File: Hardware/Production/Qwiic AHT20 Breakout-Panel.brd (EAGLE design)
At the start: 149.1 x 149.1 mm, 980 parts, among them J1 QWIIC_RIGHT_ANGLE, J10 QWIIC_RIGHT_ANGLE, J11 PTH, J12 QWIIC_RIGHT_ANGLE, J13 QWIIC_RIGHT_ANGLE, J14 PTH, J15 QWIIC_RIGHT_ANGLE, J16 QWIIC_RIGHT_ANGLE, J17 PTH, J18 QWIIC_RIGHT_ANGLE, J19 QWIIC_RIGHT_ANGLE, J2 QWIIC_RIGHT_ANGLE, J20 PTH, J21 QWIIC_RIGHT_ANGLE, J22 QWIIC_RIGHT_ANGLE, J23 PTH, J24 QWIIC_RIGHT_ANGLE, J25 QWIIC_RIGHT_ANGLE, J26 PTH, J27 QWIIC_RIGHT_ANGLE, J28 QWIIC_RIGHT_ANGLE, J29 PTH, J3 PTH, J30 QWIIC_RIGHT_ANGLE, J31 QWIIC_RIGHT_ANGLE, J32 PTH, J33 QWIIC_RIGHT_ANGLE, J34 QWIIC_RIGHT_ANGLE, J35 PTH, J36 QWIIC_RIGHT_ANGLE, J37 QWIIC_RIGHT_ANGLE, J38 PTH, J39 QWIIC_RIGHT_ANGLE, J4 QWIIC_RIGHT_ANGLE, J40 QWIIC_RIGHT_ANGLE, J41 PTH, J42 QWIIC_RIGHT_ANGLE, J43 QWIIC_RIGHT_ANGLE, J44 PTH, J45 QWIIC_RIGHT_ANGLE, J46 QWIIC_RIGHT_ANGLE, J47 PTH, J48 QWIIC_RIGHT_ANGLE, J49 QWIIC_RIGHT_ANGLE, J5 PTH, J50 PTH, J51 QWIIC_RIGHT_ANGLE, J52 QWIIC_RIGHT_ANGLE, J53 PTH, J54 QWIIC_RIGHT_ANGLE, J55 QWIIC_RIGHT_ANGLE, J56 PTH, J57 QWIIC_RIGHT_ANGLE, J58 QWIIC_RIGHT_ANGLE, J59 PTH, J6 QWIIC_RIGHT_ANGLE, J60 QWIIC_RIGHT_ANGLE, J61 QWIIC_RIGHT_ANGLE, J62 PTH, J63 QWIIC_RIGHT_ANGLE, J64 QWIIC_RIGHT_ANGLE, J65 PTH, J66 QWIIC_RIGHT_ANGLE, J67 QWIIC_RIGHT_ANGLE, J68 PTH, J69 QWIIC_RIGHT_ANGLE, J7 QWIIC_RIGHT_ANGLE, J70 QWIIC_RIGHT_ANGLE, J71 PTH, J72 QWIIC_RIGHT_ANGLE, J73 QWIIC_RIGHT_ANGLE, J74 PTH, J75 QWIIC_RIGHT_ANGLE, J8 PTH, J9 QWIIC_RIGHT_ANGLE, U1 AHT20QFN-6, U10 AHT20QFN-6, U11 AHT20QFN-6, U12 AHT20QFN-6, U13 AHT20QFN-6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

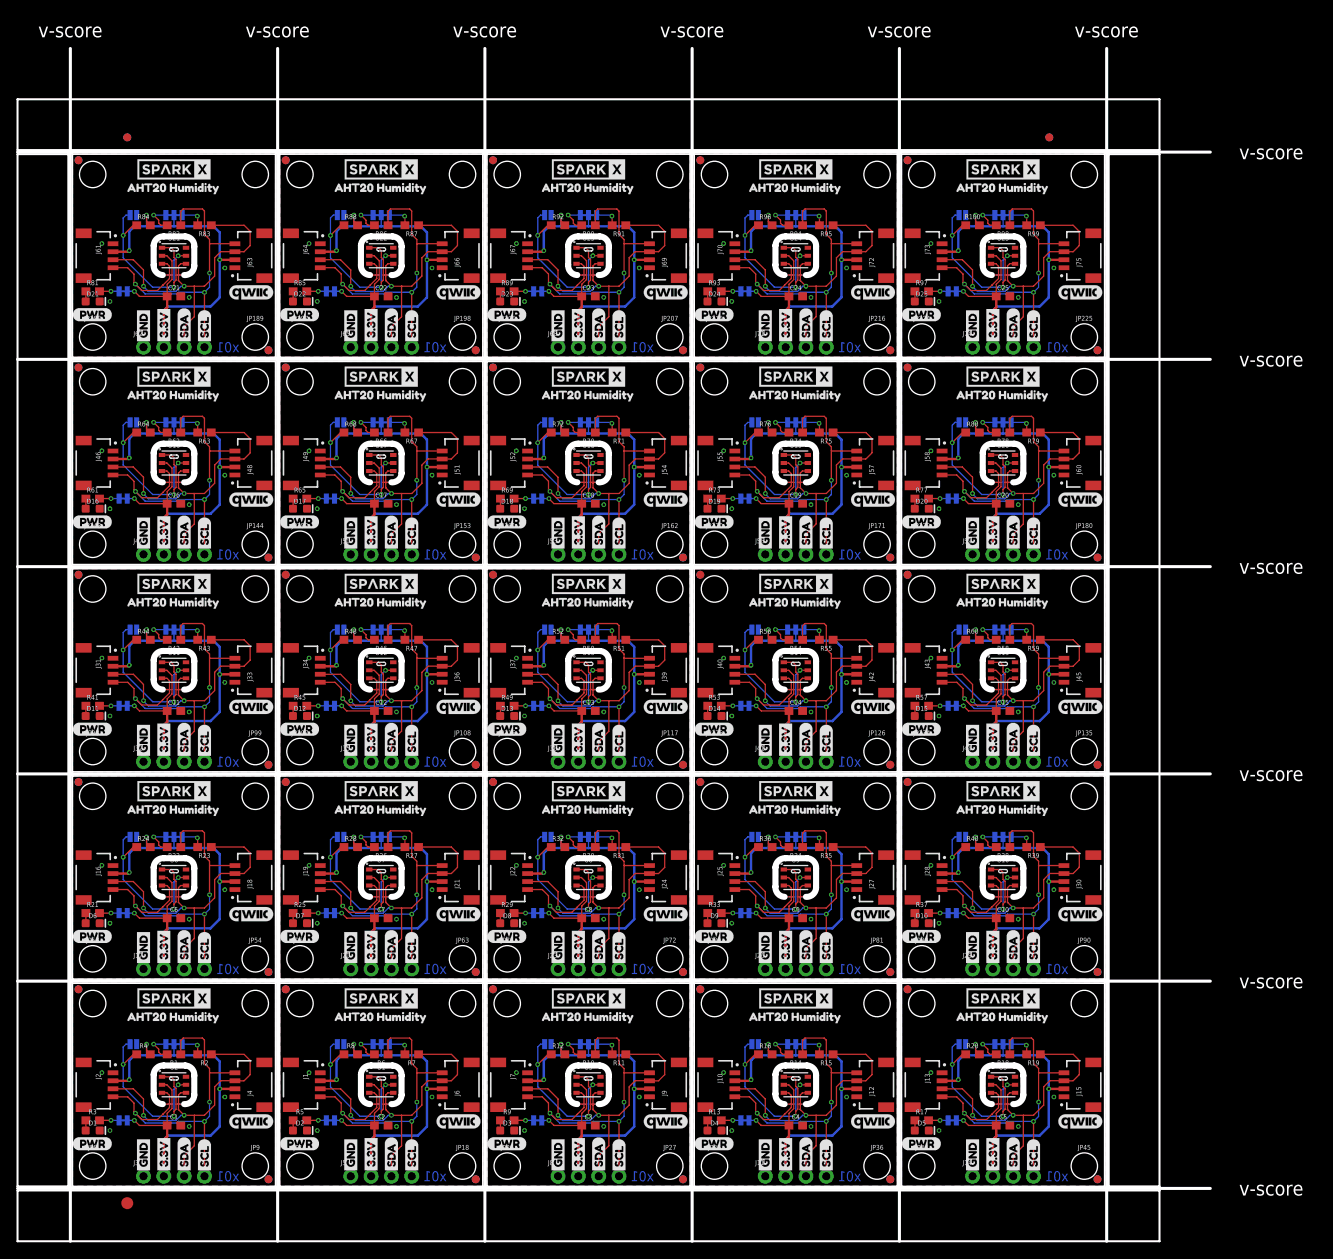
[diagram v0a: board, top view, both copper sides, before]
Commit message: Fix FP spacing. Remove experimental ADR feature. Update version number.
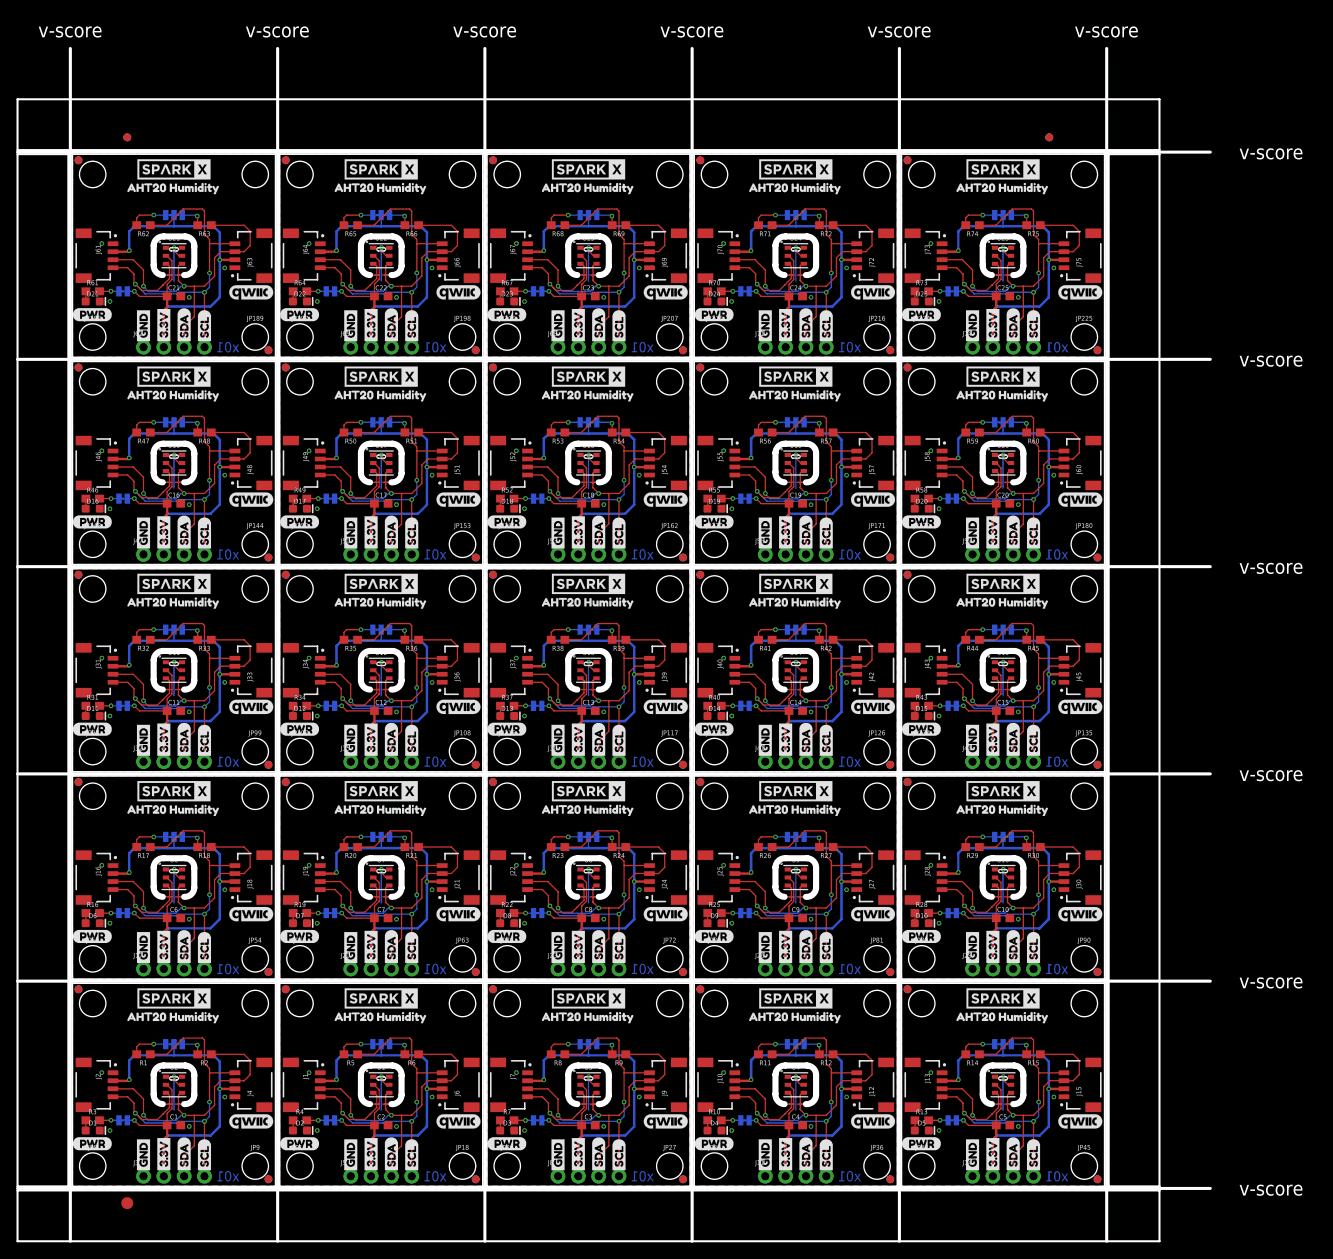
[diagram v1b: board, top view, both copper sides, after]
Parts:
- removed ADR, ADR1, ADR10, ADR11, ADR12, ADR13, ADR14, ADR15, ADR16, ADR17, ADR18, ADR19, ADR2, ADR20, ADR21, ADR22, ADR23, ADR24, ADR3, ADR4, ADR5, ADR6, ADR7, ADR8, ADR9: (no value), SparkFun-Jumpers:SMT-JUMPER_2_NO_SILK
- removed R100, R76, R80, R84, R88, R92, R96: 10k, SparkFun-Resistors:0603
- removed R77, R81, R85, R89, R93, R97: 1k, SparkFun-Resistors:0603
- removed R78, R79, R82, R83, R86, R87, R90, R91, R94, R95, R98, R99: 2.2k, SparkFun-Resistors:0603
- removed U$401, U$413, U$418: (no value), Labels-0_04:SCL9
- removed U$402, U$419: (no value), Labels-0_04:(PWR)
- removed U$403, U$420: (no value), Labels:I_SUPER2_C-()-03
- removed U$404, U$421: (no value), SparkFun-Aesthetics:QWIIC_5.5MM
- removed U$405, U$422: (no value), Labels:ADR-()-03
- removed U$406, U$408, U$423, U$425: (no value), buzzard_labels (17):AHT20_HUMIDITY2
- removed U$407, U$424: (no value), SparkFun-Buzzard:LED_32
- removed U$409, U$410: SPARKX-LOGO4, SparkX:SPARKX-MEDIUM
- removed U$411, U$416: (no value), Labels-0_04:3#3V2
- removed U$412, U$415: (no value), Labels-0_04:GND1
- removed U$414, U$417: (no value), Labels-0_04:SDA8
- LED, LED1, LED10, LED11, LED12, LED13, LED14, LED15, LED16, LED17, LED18, LED19, LED2, LED20, LED21, LED22, LED23, LED24, LED3, LED4, LED5, LED6, LED7, LED8, LED9: value (none) -> JUMPER-SMT_2_NC_TRACE_SILK
- R10, R19, R22, R31, R34, R43, R46, R55, R58, R67, R7, R70: value 2.2k -> 1k
- R12, R20, R24, R32, R36, R44, R48, R56, R60, R68, R72, R8: value 10k -> 2.2k
- R16, R28, R4, R40, R52, R64: value 10k -> 1k
- R17, R21, R29, R33, R41, R45, R5, R53, R57, R65, R69, R9: value 1k -> 2.2k
- U$100, U$119, U$151, U$340, U$372, U$391, U$68: device buzzard_labels (17):AHT20_HUMIDITY2 -> Labels-0_04:GND1
- U$101, U$186, U$373: device SparkFun-Buzzard:LED_32 -> Labels-0_04:SCL9
- U$102, U$134, U$153, U$185, U$374: device buzzard_labels (17):AHT20_HUMIDITY2 -> Labels-0_04:SDA8
- U$103, U$308, U$324, U$359, U$36, U$375, U$52, U$87: value SPARKX-LOGO4 -> (none); device SparkX:SPARKX-MEDIUM -> Labels-0_04:GND1
- U$104, U$120, U$15, U$291, U$307, U$35, U$376, U$392: value SPARKX-LOGO4 -> (none); device SparkX:SPARKX-MEDIUM -> Labels-0_04:3#3V2
- U$105, U$23, U$246, U$297, U$326, U$377, U$54: device Labels-0_04:3#3V2 -> Labels-0_04:SDA8
- U$106, U$17, U$245, U$293, U$330, U$378, U$58: device Labels-0_04:GND1 -> Labels-0_04:SCL9
- U$107, U$25, U$299, U$379: device Labels-0_04:SCL9 -> Labels-0_04:(PWR)
- U$108, U$332, U$380, U$60: device Labels-0_04:SDA8 -> Labels:I_SUPER2_C-()-03
- U$109, U$157, U$381: device Labels-0_04:GND1 -> SparkFun-Aesthetics:QWIIC_5.5MM
- U$110, U$144, U$190, U$224, U$382: device Labels-0_04:3#3V2 -> buzzard_labels (17):AHT20_HUMIDITY2
- U$111, U$159, U$383: device Labels-0_04:SDA8 -> SparkFun-Buzzard:LED_32
- U$112, U$158, U$192, U$350, U$384, U$78: device Labels-0_04:SCL9 -> buzzard_labels (17):AHT20_HUMIDITY2
- U$113, U$130, U$385: value (none) -> SPARKX-LOGO4; device Labels-0_04:(PWR) -> SparkX:SPARKX-MEDIUM
- U$114, U$369, U$386, U$97: value (none) -> SPARKX-LOGO4; device Labels:I_SUPER2_C-()-03 -> SparkX:SPARKX-MEDIUM
- U$115, U$200, U$387: device SparkFun-Aesthetics:QWIIC_5.5MM -> Labels-0_04:3#3V2
- U$116, U$167, U$388: device Labels:ADR-()-03 -> Labels-0_04:GND1
- U$117, U$170, U$202, U$357, U$389, U$85: device buzzard_labels (17):AHT20_HUMIDITY2 -> Labels-0_04:SCL9
- U$118, U$169, U$390: device SparkFun-Buzzard:LED_32 -> Labels-0_04:SDA8
- U$121, U$137, U$342, U$358, U$393, U$70, U$86: value SPARKX-LOGO4 -> (none); device SparkX:SPARKX-MEDIUM -> Labels-0_04:SDA8
- U$122, U$229, U$309, U$314, U$37, U$394, U$42: device Labels-0_04:3#3V2 -> Labels-0_04:SCL9
- U$123, U$347, U$395, U$75: device Labels-0_04:GND1 -> Labels-0_04:(PWR)
- U$124, U$316, U$396, U$44: device Labels-0_04:SCL9 -> Labels:I_SUPER2_C-()-03
- U$125, U$349, U$397, U$77: device Labels-0_04:SDA8 -> SparkFun-Aesthetics:QWIIC_5.5MM
- U$126, U$160, U$174, U$208, U$398: device Labels-0_04:GND1 -> buzzard_labels (17):AHT20_HUMIDITY2
- U$127, U$207, U$399: device Labels-0_04:3#3V2 -> SparkFun-Buzzard:LED_32
- U$128, U$142, U$176, U$366, U$400, U$94: device Labels-0_04:SDA8 -> buzzard_labels (17):AHT20_HUMIDITY2
- U$129, U$146, U$209, U$226: value (none) -> SPARKX-LOGO4; device Labels-0_04:SCL9 -> SparkX:SPARKX-MEDIUM
- U$13, U$337, U$354, U$65, U$82: value (none) -> SPARKX-LOGO4; device Labels:ADR-()-03 -> SparkX:SPARKX-MEDIUM
- U$131, U$216: device Labels:I_SUPER2_C-()-03 -> Labels-0_04:3#3V2
- U$132, U$183: device SparkFun-Aesthetics:QWIIC_5.5MM -> Labels-0_04:GND1
- U$133, U$218: device Labels:ADR-()-03 -> Labels-0_04:SCL9
- U$135, U$356, U$84: device SparkFun-Buzzard:LED_32 -> Labels-0_04:GND1
- U$136, U$168, U$323, U$355, U$51, U$83: device buzzard_labels (17):AHT20_HUMIDITY2 -> Labels-0_04:3#3V2
- U$138, U$154, U$325, U$341, U$53, U$69: value SPARKX-LOGO4 -> (none); device SparkX:SPARKX-MEDIUM -> Labels-0_04:SCL9
- U$139, U$331, U$59: device Labels-0_04:3#3V2 -> Labels-0_04:(PWR)
- U$140, U$364, U$92: device Labels-0_04:GND1 -> Labels:I_SUPER2_C-()-03
- U$141, U$333, U$61: device Labels-0_04:SCL9 -> SparkFun-Aesthetics:QWIIC_5.5MM
- U$143, U$191: device Labels-0_04:GND1 -> SparkFun-Buzzard:LED_32
- U$145, U$162, U$193, U$210: value (none) -> SPARKX-LOGO4; device Labels-0_04:SDA8 -> SparkX:SPARKX-MEDIUM
- U$147, U$232: device Labels-0_04:(PWR) -> Labels-0_04:3#3V2
- U$148, U$199: device Labels:I_SUPER2_C-()-03 -> Labels-0_04:GND1
- U$149, U$234: device SparkFun-Aesthetics:QWIIC_5.5MM -> Labels-0_04:SCL9
- U$150, U$201: device Labels:ADR-()-03 -> Labels-0_04:SDA8
- U$152, U$339, U$67: device SparkFun-Buzzard:LED_32 -> Labels-0_04:3#3V2
- U$155, U$171: value SPARKX-LOGO4 -> (none); device SparkX:SPARKX-MEDIUM -> Labels-0_04:(PWR)
- U$156, U$348, U$76: device Labels-0_04:3#3V2 -> Labels:I_SUPER2_C-()-03
- U$16, U$212, U$263, U$292, U$343, U$71: device Labels-0_04:3#3V2 -> Labels-0_04:GND1
- U$161, U$178, U$241, U$258: value (none) -> SPARKX-LOGO4; device Labels-0_04:3#3V2 -> SparkX:SPARKX-MEDIUM
- U$163, U$243, U$248, U$328, U$56: device Labels-0_04:SCL9 -> Labels-0_04:3#3V2
- U$164, U$215: device Labels-0_04:(PWR) -> Labels-0_04:GND1
- U$165, U$250: device Labels:I_SUPER2_C-()-03 -> Labels-0_04:SCL9
- U$166, U$217: device SparkFun-Aesthetics:QWIIC_5.5MM -> Labels-0_04:SDA8
- U$172, U$188: value SPARKX-LOGO4 -> (none); device SparkX:SPARKX-MEDIUM -> Labels:I_SUPER2_C-()-03
- U$173, U$365, U$93: device Labels-0_04:3#3V2 -> SparkFun-Aesthetics:QWIIC_5.5MM
- U$175, U$367, U$95: device Labels-0_04:SCL9 -> SparkFun-Buzzard:LED_32
- U$177, U$194, U$225, U$242: value (none) -> SPARKX-LOGO4; device Labels-0_04:GND1 -> SparkX:SPARKX-MEDIUM
- U$179, U$227, U$264, U$312, U$40: device Labels-0_04:SDA8 -> Labels-0_04:3#3V2
- U$18, U$214, U$265, U$294, U$345, U$73: device Labels-0_04:SCL9 -> Labels-0_04:SDA8
- U$180, U$231, U$260, U$311, U$39: device Labels-0_04:SCL9 -> Labels-0_04:GND1
- U$181, U$266: device Labels-0_04:(PWR) -> Labels-0_04:SCL9
- U$182, U$233: device Labels:I_SUPER2_C-()-03 -> Labels-0_04:SDA8
- U$184, U$371, U$99: device Labels:ADR-()-03 -> Labels-0_04:3#3V2
- U$187, U$219: device buzzard_labels (17):AHT20_HUMIDITY2 -> Labels-0_04:(PWR)
- U$189, U$205: value SPARKX-LOGO4 -> (none); device SparkX:SPARKX-MEDIUM -> SparkFun-Aesthetics:QWIIC_5.5MM
- U$19, U$196, U$244, U$247, U$295: device Labels-0_04:SDA8 -> Labels-0_04:GND1
- U$198, U$249: device Labels-0_04:(PWR) -> Labels-0_04:SDA8
- U$20, U$211, U$259, U$296, U$344, U$72: device Labels-0_04:GND1 -> Labels-0_04:3#3V2
- U$203: device SparkFun-Buzzard:LED_32 -> Labels-0_04:(PWR)
- U$204, U$236: device buzzard_labels (17):AHT20_HUMIDITY2 -> Labels:I_SUPER2_C-()-03
- U$206, U$222, U$240, U$256: value SPARKX-LOGO4 -> (none); device SparkX:SPARKX-MEDIUM -> buzzard_labels (17):AHT20_HUMIDITY2
- U$213, U$24, U$261, U$298, U$346, U$74: device Labels-0_04:SDA8 -> Labels-0_04:SCL9
- U$220: device SparkFun-Buzzard:LED_32 -> Labels:I_SUPER2_C-()-03
- U$221, U$253: device buzzard_labels (17):AHT20_HUMIDITY2 -> SparkFun-Aesthetics:QWIIC_5.5MM
- U$223, U$239: value SPARKX-LOGO4 -> (none); device SparkX:SPARKX-MEDIUM -> SparkFun-Buzzard:LED_32
- U$235: device Labels:ADR-()-03 -> Labels-0_04:(PWR)
- U$237: device SparkFun-Buzzard:LED_32 -> SparkFun-Aesthetics:QWIIC_5.5MM
- U$251: device SparkFun-Aesthetics:QWIIC_5.5MM -> Labels-0_04:(PWR)
- U$252: device Labels:ADR-()-03 -> Labels:I_SUPER2_C-()-03
- U$254, U$288: device SparkFun-Buzzard:LED_32 -> buzzard_labels (17):AHT20_HUMIDITY2
- U$255, U$287: device buzzard_labels (17):AHT20_HUMIDITY2 -> SparkFun-Buzzard:LED_32
- U$262, U$310, U$313, U$361, U$38, U$41, U$89: device Labels-0_04:GND1 -> Labels-0_04:SDA8
- U$267: device Labels:I_SUPER2_C-()-03 -> Labels-0_04:(PWR)
- U$268: device SparkFun-Aesthetics:QWIIC_5.5MM -> Labels:I_SUPER2_C-()-03
- U$269: device Labels:ADR-()-03 -> SparkFun-Aesthetics:QWIIC_5.5MM
- U$28, U$300: device Labels-0_04:(PWR) -> Labels:I_SUPER2_C-()-03
- U$286, U$320, U$48: device Labels:ADR-()-03 -> buzzard_labels (17):AHT20_HUMIDITY2
- U$289, U$306, U$321, U$338, U$34, U$49, U$66: value (none) -> SPARKX-LOGO4; device buzzard_labels (17):AHT20_HUMIDITY2 -> SparkX:SPARKX-MEDIUM
- U$29, U$301: device Labels:I_SUPER2_C-()-03 -> SparkFun-Aesthetics:QWIIC_5.5MM
- U$30, U$302, U$336, U$64: device SparkFun-Aesthetics:QWIIC_5.5MM -> buzzard_labels (17):AHT20_HUMIDITY2
- U$303, U$31: device Labels:ADR-()-03 -> SparkFun-Buzzard:LED_32
- U$305, U$322, U$33, U$50: value (none) -> SPARKX-LOGO4; device SparkFun-Buzzard:LED_32 -> SparkX:SPARKX-MEDIUM
- U$315, U$363, U$43, U$91: device Labels-0_04:SDA8 -> Labels-0_04:(PWR)
- U$317, U$45: device Labels-0_04:(PWR) -> SparkFun-Aesthetics:QWIIC_5.5MM
- U$318, U$352, U$46, U$80: device Labels:I_SUPER2_C-()-03 -> buzzard_labels (17):AHT20_HUMIDITY2
- U$319, U$47: device SparkFun-Aesthetics:QWIIC_5.5MM -> SparkFun-Buzzard:LED_32
- U$334, U$368, U$62, U$96: device Labels-0_04:(PWR) -> buzzard_labels (17):AHT20_HUMIDITY2
- U$335, U$63: device Labels:I_SUPER2_C-()-03 -> SparkFun-Buzzard:LED_32
- U$351, U$79: device Labels-0_04:(PWR) -> SparkFun-Buzzard:LED_32
- U$353, U$370, U$81, U$98: value (none) -> SPARKX-LOGO4; device SparkFun-Aesthetics:QWIIC_5.5MM -> SparkX:SPARKX-MEDIUM
- moved U$251 128.1 mm to (0.00, 83.1)
- moved U$81 120.6 mm to (12.7, 49.4), flipped to the bottom
- moved U$331 118.8 mm to (0.00, 109.0), flipped to the top, turned to 0 degrees
- moved U$255 115.3 mm to (8.13, 83.9)
- moved U$162 115.3 mm to (12.7, 75.3), flipped to the top, turned to 0 degrees
- moved U$166 113.7 mm to (14.0, 53.3), turned to 90 degrees
- moved U$336 113.6 mm to (19.3, 124.8), flipped to the bottom
- moved U$254 113.4 mm to (5.97, 98.9), flipped to the top
- moved U$161 113.0 mm to (12.7, 75.3), turned to 0 degrees
- moved U$241 113.0 mm to (12.7, 101.2), flipped to the bottom, turned to 0 degrees
- moved U$332 112.5 mm to (14.1, 123.3), turned to 0 degrees
- moved U$244 111.8 mm to (8.89, 79.2)
- moved U$247 111.8 mm to (8.89, 79.2)
- moved U$163 111.8 mm to (11.4, 53.3), flipped to the top
- moved U$243 111.8 mm to (11.4, 79.2)
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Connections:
- removed net N$10: LED1.1, R5.2
- removed net N$100: LED16.1, R65.2
- removed net N$105: JP160.1, R71.2
- removed net N$110: JP169.3, R74.2
- removed net N$115: D20.A, R77.1
- removed net N$125: ADR20.2, R84.1, U21.ADR
- removed net N$127: D22.A, R85.1
- removed net N$128: JP196.3, R86.2
- removed net N$129: JP196.1, R87.2
- removed net N$130: LED21.1, R85.2
- removed net N$131: ADR21.2, R88.1, U22.ADR
- removed net N$133: D23.A, R89.1
- removed net N$134: JP205.3, R90.2
- removed net N$135: JP205.1, R91.2
- removed net N$136: LED22.1, R89.2
- removed net N$137: ADR22.2, R92.1, U23.ADR
- removed net N$139: D24.A, R93.1
- removed net N$140: JP214.3, R94.2
- removed net N$141: JP214.1, R95.2
- removed net N$142: LED23.1, R93.2
- removed net N$143: ADR23.2, R96.1, U24.ADR
- removed net N$145: D25.A, R97.1
- removed net N$146: JP223.3, R98.2
- removed net N$147: JP223.1, R99.2
- removed net N$148: LED24.1, R97.2
- removed net N$149: ADR24.2, R100.1, U25.ADR
- removed net N$15: JP25.1, R11.2
- removed net N$20: JP34.3, R14.2
- removed net N$25: D5.A, R17.1
- removed net N$35: ADR5.2, R24.1, U6.ADR
- removed net N$40: LED6.1, R25.2
- removed net N$45: JP70.1, R31.2
- removed net N$50: JP79.3, R34.2
- removed net N$55: D10.A, R37.1
- removed net N$65: ADR10.2, R44.1, U11.ADR
- removed net N$70: LED11.1, R45.2
- removed net N$75: JP115.1, R51.2
- removed net N$80: JP124.3, R54.2
- removed net N$85: D15.A, R57.1
- removed net N$95: ADR15.2, R64.1, U16.ADR
- new net N$102: JP187.3, R62.2
- new net N$108: JP196.1, R66.2
- new net N$114: LED22.1, R67.2
- new net N$12: JP25.3, R8.2
- new net N$18: JP34.1, R12.2
- new net N$24: LED4.1, R13.2
- new net N$36: D8.A, R22.1
- new net N$42: JP79.3, R26.2
- new net N$48: JP88.1, R30.2
- new net N$54: LED10.1, R31.2
- new net N$66: D14.A, R40.1
- new net N$72: JP133.3, R44.2
- new net N$78: JP142.1, R48.2
- new net N$84: LED16.1, R49.2
- new net N$96: D20.A, R58.1
- net 3.3V: no longer R4.2
- net 3.3V1: no longer R8.2
- net 3.3V10: no longer R44.2
- net 3.3V11: no longer R48.2
- net 3.3V12: no longer R52.2
- net 3.3V13: no longer R56.2
- net 3.3V14: no longer R60.2
- net 3.3V15: no longer R64.2
- net 3.3V16: no longer R68.2
- net 3.3V17: no longer R72.2
- net 3.3V18: no longer R76.2
- net 3.3V19: no longer R80.2
- net 3.3V2: no longer R12.2
- net 3.3V20: no longer R84.2
- net 3.3V21: no longer R88.2
- net 3.3V22: no longer R92.2
- net 3.3V23: no longer R96.2
- net 3.3V24: no longer R100.2
- net 3.3V3: no longer R16.2
- net 3.3V4: no longer R20.2
- net 3.3V5: no longer R24.2
- net 3.3V6: no longer R28.2
- net 3.3V7: no longer R32.2
- net 3.3V8: no longer R36.2
- net 3.3V9: no longer R40.2
- net GND: no longer ADR.1
- net GND1: no longer ADR1.1
- net GND10: no longer ADR10.1
- net GND11: no longer ADR11.1
- net GND12: no longer ADR12.1
- net GND13: no longer ADR13.1
- net GND14: no longer ADR14.1
- net GND15: no longer ADR15.1
- net GND16: no longer ADR16.1
- net GND17: no longer ADR17.1
- net GND18: no longer ADR18.1
- net GND19: no longer ADR19.1
- net GND2: no longer ADR2.1
- net GND20: no longer ADR20.1
- net GND21: no longer ADR21.1
- net GND22: no longer ADR22.1
- net GND23: no longer ADR23.1
- net GND24: no longer ADR24.1
- net GND3: no longer ADR3.1
- net GND4: no longer ADR4.1
- net GND5: no longer ADR5.1
- net GND6: no longer ADR6.1
- net GND7: no longer ADR7.1
- net GND8: no longer ADR8.1
- net GND9: no longer ADR9.1
- net N$101: now also D21.A, R61.1; no longer ADR16.2, R68.1, U17.ADR
- net N$103: now also JP187.1, R63.2; no longer D18.A, R69.1
- net N$104: now also LED20.1, R61.2; no longer JP160.3, R70.2
- net N$106: now also D22.A, R64.1; no longer LED17.1, R69.2
- net N$107: now also JP196.3, R65.2; no longer ADR17.2, R72.1, U18.ADR
- net N$109: now also LED21.1, R64.2; no longer D19.A, R73.1
- net N$11: now also D3.A, R7.1; no longer ADR1.2, R8.1, U1.ADR
- net N$111: now also D23.A, R67.1; no longer JP169.1, R75.2
- net N$112: now also JP205.3, R68.2; no longer LED18.1, R73.2
- net N$113: now also JP205.1, R69.2; no longer ADR18.2, R76.1, U19.ADR
- net N$116: now also D24.A, R70.1; no longer JP178.3, R78.2
- net N$117: now also JP214.3, R71.2; no longer JP178.1, R79.2
- net N$118: now also JP214.1, R72.2; no longer LED19.1, R77.2
- net N$119: now also LED23.1, R70.2; no longer ADR19.2, R80.1, U20.ADR
- net N$121: now also D25.A, R73.1; no longer D21.A, R81.1
- net N$122: now also JP223.3, R74.2; no longer JP187.3, R82.2
- net N$123: now also JP223.1, R75.2; no longer JP187.1, R83.2
- net N$124: now also LED24.1, R73.2; no longer LED20.1, R81.2
- net N$13: now also JP25.1, R9.2; no longer D3.A, R9.1
- net N$14: now also LED2.1, R7.2; no longer JP25.3, R10.2
- net N$16: now also D4.A, R10.1; no longer LED2.1, R9.2
- net N$17: now also JP34.3, R11.2; no longer ADR2.2, R12.1, U3.ADR
- net N$19: now also LED3.1, R10.2; no longer D4.A, R13.1
- net N$21: now also D5.A, R13.1; no longer JP34.1, R15.2
- net N$22: now also JP43.3, R14.2; no longer LED3.1, R13.2
- net N$23: now also JP43.1, R15.2; no longer ADR3.2, R16.1, U4.ADR
- net N$26: now also D6.A, R16.1; no longer JP43.3, R18.2
- net N$27: now also JP52.3, R17.2; no longer JP43.1, R19.2
- net N$28: now also JP52.1, R18.2; no longer LED4.1, R17.2
- net N$29: now also LED5.1, R16.2; no longer ADR4.2, R20.1, U5.ADR
- net N$31: now also D7.A, R19.1; no longer D6.A, R21.1
- net N$32: now also JP61.3, R20.2; no longer JP52.3, R22.2
- net N$33: now also JP61.1, R21.2; no longer JP52.1, R23.2
- net N$34: now also LED6.1, R19.2; no longer LED5.1, R21.2
- net N$37: now also JP70.3, R23.2; no longer D7.A, R25.1
- net N$38: now also JP70.1, R24.2; no longer JP61.3, R26.2
- net N$39: now also LED7.1, R22.2; no longer JP61.1, R27.2
- net N$41: now also D9.A, R25.1; no longer ADR6.2, R28.1, U7.ADR
- net N$43: now also JP79.1, R27.2; no longer D8.A, R29.1
- net N$44: now also LED8.1, R25.2; no longer JP70.3, R30.2
- net N$46: now also D10.A, R28.1; no longer LED7.1, R29.2
- net N$47: now also JP88.3, R29.2; no longer ADR7.2, R32.1, U8.ADR
- net N$49: now also LED9.1, R28.2; no longer D9.A, R33.1
- net N$5: now also D2.A; no longer ADR.2, U2.ADR
- net N$51: now also D11.A, R31.1; no longer JP79.1, R35.2
- net N$52: now also JP97.3, R32.2; no longer LED8.1, R33.2
- net N$53: now also JP97.1, R33.2; no longer ADR8.2, R36.1, U9.ADR
- net N$56: now also D12.A, R34.1; no longer JP88.3, R38.2
- net N$57: now also JP106.3, R35.2; no longer JP88.1, R39.2
- net N$58: now also JP106.1, R36.2; no longer LED9.1, R37.2
- net N$59: now also LED11.1, R34.2; no longer ADR9.2, R40.1, U10.ADR
- net N$61: now also D13.A, R37.1; no longer D11.A, R41.1
- net N$62: now also JP115.3, R38.2; no longer JP97.3, R42.2
- net N$63: now also JP115.1, R39.2; no longer JP97.1, R43.2
- net N$64: now also LED12.1, R37.2; no longer LED10.1, R41.2
- net N$67: now also JP124.3, R41.2; no longer D12.A, R45.1
- net N$68: now also JP124.1, R42.2; no longer JP106.3, R46.2
- net N$69: now also LED13.1, R40.2; no longer JP106.1, R47.2
- net N$7: now also JP16.3, R5.2; no longer D2.A, R5.1
- net N$71: now also D15.A, R43.1; no longer ADR11.2, R48.1, U12.ADR
- net N$73: now also JP133.1, R45.2; no longer D13.A, R49.1
- net N$74: now also LED14.1, R43.2; no longer JP115.3, R50.2
- net N$76: now also D16.A, R46.1; no longer LED12.1, R49.2
- net N$77: now also JP142.3, R47.2; no longer ADR12.2, R52.1, U13.ADR
- net N$79: now also LED15.1, R46.2; no longer D14.A, R53.1
- net N$8: now also JP16.1; no longer JP16.3
- net N$81: now also D17.A, R49.1; no longer JP124.1, R55.2
- net N$82: now also JP151.3, R50.2; no longer LED13.1, R53.2
- net N$83: now also JP151.1, R51.2; no longer ADR13.2, R56.1, U14.ADR
- net N$86: now also D18.A, R52.1; no longer JP133.3, R58.2
- net N$87: now also JP160.3, R53.2; no longer JP133.1, R59.2
- net N$88: now also JP160.1, R54.2; no longer LED14.1, R57.2
- net N$89: now also LED17.1, R52.2; no longer ADR14.2, R60.1, U15.ADR
- net N$9: now also LED1.1, R4.2; no longer JP16.1, R7.2
- net N$91: now also D19.A, R55.1; no longer D16.A, R61.1
- net N$92: now also JP169.3, R56.2; no longer JP142.3, R62.2
- net N$93: now also JP169.1, R57.2; no longer JP142.1, R63.2
- net N$94: now also LED18.1, R55.2; no longer LED15.1, R61.2
- net N$97: now also JP178.3, R59.2; no longer D17.A, R65.1
- net N$98: now also JP178.1, R60.2; no longer JP151.3, R66.2
- net N$99: now also LED19.1, R58.2; no longer JP151.1, R67.2
- net SCL1: now also R5.1; no longer R6.1
- net SCL10: now also R32.1; no longer R42.1
- net SCL11: now also R35.1; no longer R46.1
- net SCL12: now also R38.1; no longer R50.1
- net SCL13: now also R41.1; no longer R54.1
- net SCL14: now also R44.1; no longer R58.1
- net SCL15: now also R47.1; no longer R62.1
- net SCL16: now also R50.1; no longer R66.1
- net SCL17: now also R53.1; no longer R70.1
- net SCL18: now also R56.1; no longer R74.1
- net SCL19: now also R59.1; no longer R78.1
- net SCL2: now also R8.1; no longer R10.1
- net SCL20: now also R62.1; no longer R82.1
- net SCL21: now also R65.1; no longer R86.1
- net SCL22: now also R68.1; no longer R90.1
- net SCL23: now also R71.1; no longer R94.1
- net SCL24: now also R74.1; no longer R98.1
- net SCL3: now also R11.1; no longer R14.1
- net SCL4: now also R14.1; no longer R18.1
- net SCL5: now also R17.1; no longer R22.1
- net SCL6: now also R20.1; no longer R26.1
- net SCL7: now also R23.1; no longer R30.1
- net SCL8: now also R26.1; no longer R34.1
- net SCL9: now also R29.1; no longer R38.1
- net SDA1: now also R6.1; no longer R7.1
- net SDA10: now also R33.1; no longer R43.1
- net SDA11: now also R36.1; no longer R47.1
- net SDA12: now also R39.1; no longer R51.1
- net SDA13: now also R42.1; no longer R55.1
- net SDA14: now also R45.1; no longer R59.1
- net SDA15: now also R48.1; no longer R63.1
- net SDA16: now also R51.1; no longer R67.1
- net SDA17: now also R54.1; no longer R71.1
- net SDA18: now also R57.1; no longer R75.1
- net SDA19: now also R60.1; no longer R79.1
- net SDA2: now also R9.1; no longer R11.1
- net SDA20: now also R63.1; no longer R83.1
- net SDA21: now also R66.1; no longer R87.1
- net SDA22: now also R69.1; no longer R91.1
- net SDA23: now also R72.1; no longer R95.1
- net SDA24: now also R75.1; no longer R99.1
- net SDA3: now also R12.1; no longer R15.1
- net SDA4: now also R15.1; no longer R19.1
- net SDA5: now also R18.1; no longer R23.1
- net SDA6: now also R21.1; no longer R27.1
- net SDA7: now also R24.1; no longer R31.1
- net SDA8: now also R27.1; no longer R35.1
- net SDA9: now also R30.1; no longer R39.1
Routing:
- net N$95: track 22.5 -> 0.00 mm, vias 2 -> 0
- net N$137: track 22.5 -> 0.00 mm, vias 2 -> 0
- net N$149: track 22.5 -> 0.00 mm, vias 2 -> 0
- net N$131: track 22.5 -> 0.00 mm, vias 2 -> 0
- net N$125: track 22.5 -> 0.00 mm, vias 2 -> 0
- net N$65: track 22.5 -> 0.00 mm, vias 2 -> 0
- net N$35: track 22.5 -> 0.00 mm, vias 2 -> 0
- net N$143: track 22.5 -> 0.00 mm, vias 2 -> 0
- net N$101: track 22.5 -> 1.28 mm, vias 2 -> 0
- net N$11: track 22.5 -> 1.28 mm, vias 2 -> 0
- net N$5: track 22.5 -> 1.28 mm, vias 2 -> 0
- net N$71: track 22.5 -> 1.28 mm, vias 2 -> 0
- net N$41: track 22.5 -> 1.28 mm, vias 2 -> 0
- net N$119: track 22.5 -> 2.44 mm, vias 2 -> 1
- net N$29: track 22.5 -> 2.44 mm, vias 2 -> 1
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- added copper zone on layer 1, net N$10
- added copper zone on layer 16, net N$10
- added copper zone on layer 1, net N$100
- added copper zone on layer 16, net N$100
- added copper zone on layer 1, net N$105
- added copper zone on layer 16, net N$105
- added copper zone on layer 1, net N$110
- added copper zone on layer 16, net N$110
- added copper zone on layer 1, net N$115
- added copper zone on layer 16, net N$115
- added copper zone on layer 1, net N$125
- added copper zone on layer 16, net N$125
- added copper zone on layer 1, net N$15
- added copper zone on layer 16, net N$15
- added copper zone on layer 1, net N$20
- added copper zone on layer 16, net N$20
- added copper zone on layer 1, net N$25
- added copper zone on layer 16, net N$25
- added copper zone on layer 1, net N$35
- added copper zone on layer 16, net N$35
- added copper zone on layer 1, net N$40
- added copper zone on layer 16, net N$40
- added copper zone on layer 1, net N$45
- added copper zone on layer 16, net N$45
- added copper zone on layer 1, net N$50
- added copper zone on layer 16, net N$50
- added copper zone on layer 1, net N$55
- added copper zone on layer 16, net N$55
- added copper zone on layer 1, net N$65
- added copper zone on layer 16, net N$65
- added copper zone on layer 1, net N$70
- added copper zone on layer 16, net N$70
- added copper zone on layer 1, net N$75
- added copper zone on layer 16, net N$75
- added copper zone on layer 1, net N$80
- added copper zone on layer 16, net N$80
- added copper zone on layer 1, net N$85
- added copper zone on layer 16, net N$85
- added copper zone on layer 1, net N$95
- added copper zone on layer 16, net N$95
- removed copper zone on layer 1, net N$102
- removed copper zone on layer 16, net N$102
- removed copper zone on layer 1, net N$108
- removed copper zone on layer 16, net N$108
- removed copper zone on layer 1, net N$114
- removed copper zone on layer 16, net N$114
- removed copper zone on layer 1, net N$12
- removed copper zone on layer 16, net N$12
- removed copper zone on layer 1, net N$126
- removed copper zone on layer 16, net N$126
- removed copper zone on layer 1, net N$132
- removed copper zone on layer 16, net N$132
- removed copper zone on layer 1, net N$138
- removed copper zone on layer 16, net N$138
- removed copper zone on layer 1, net N$144
- removed copper zone on layer 16, net N$144
- removed copper zone on layer 1, net N$150
- removed copper zone on layer 16, net N$150
- removed copper zone on layer 1, net N$18
- removed copper zone on layer 16, net N$18
- removed copper zone on layer 1, net N$24
- removed copper zone on layer 16, net N$24
- removed copper zone on layer 1, net N$36
- removed copper zone on layer 16, net N$36
- removed copper zone on layer 1, net N$42
- removed copper zone on layer 16, net N$42
- removed copper zone on layer 1, net N$48
- removed copper zone on layer 16, net N$48
- removed copper zone on layer 1, net N$54
- removed copper zone on layer 16, net N$54
- removed copper zone on layer 1, net N$66
- removed copper zone on layer 16, net N$66
- removed copper zone on layer 1, net N$72
- removed copper zone on layer 16, net N$72
- removed copper zone on layer 1, net N$78
- removed copper zone on layer 16, net N$78
- removed copper zone on layer 1, net N$84
- removed copper zone on layer 16, net N$84
- removed copper zone on layer 1, net N$96
- removed copper zone on layer 16, net N$96

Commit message: Add x02 panel.
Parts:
- added E$6: (no value), SparkFun-Retired:FIDUCIAL-1.5X3
- moved E$5 12.7 mm to (-2.62, 6.35)
- moved E$3 10.7 mm to (131.7, 126.4)
- moved E$4 10.7 mm to (131.7, 126.4)
- moved E$1 10.6 mm to (-2.62, 126.4)
- moved E$2 10.6 mm to (-2.62, 126.4)
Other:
- board size 149.1 x 149.1 mm -> 149.1 x 143.3 mm
- board text added: "x02"
- board text removed: "x01"
